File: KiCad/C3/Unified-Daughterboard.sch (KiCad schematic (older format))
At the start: 14 parts, among them J1 TYPE-C-31-M12_13, J2 SM04B-SRSS-TB(LF)(SN), U1 TPD4E05U06DQAR

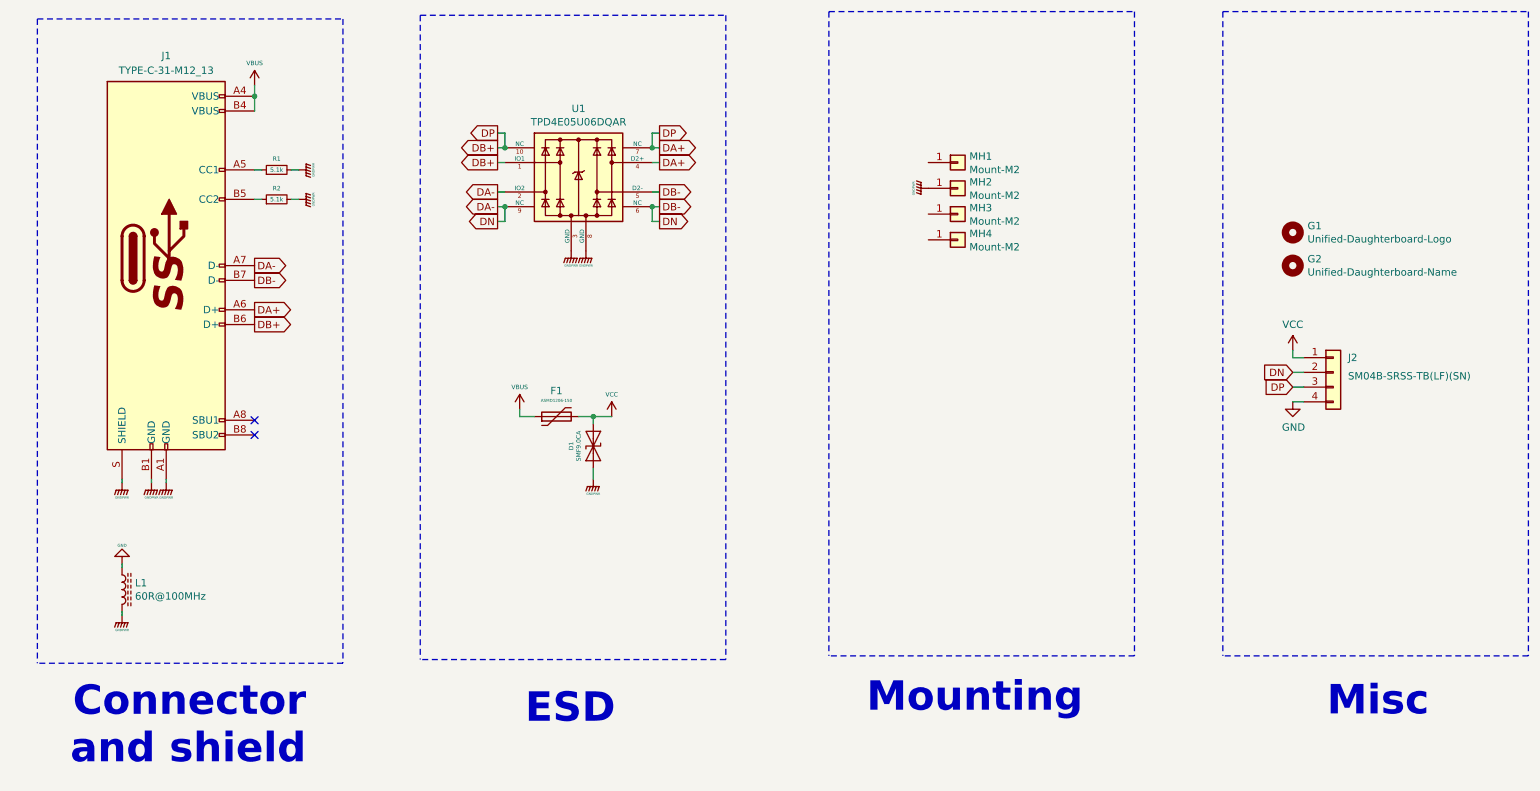
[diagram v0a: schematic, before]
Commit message: various optimizations to schematic and layout
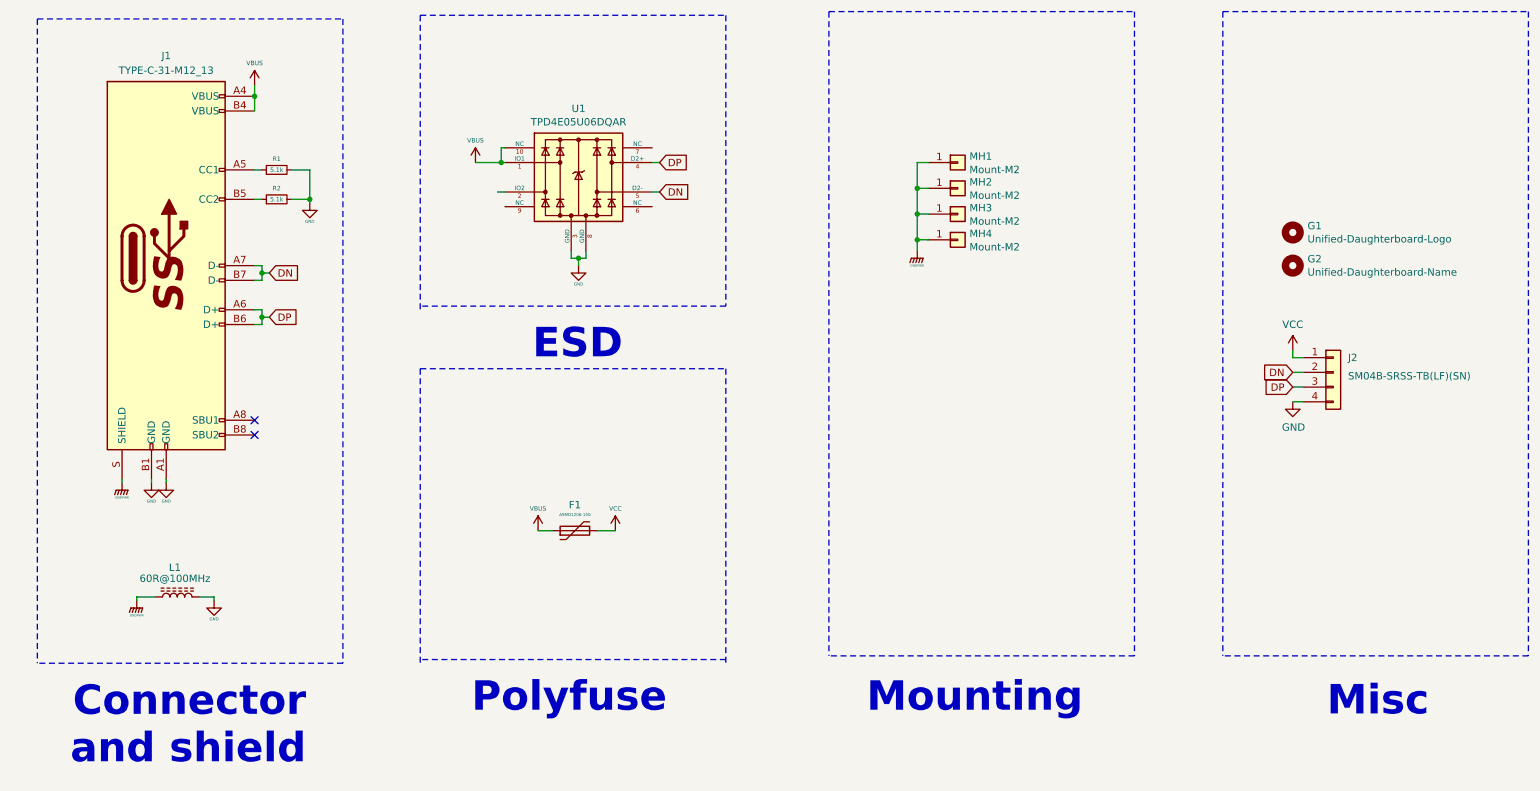
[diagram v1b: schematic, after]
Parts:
- removed D1: SMF9.0CA, acheron_Components:D_SOD-123_Bidirectional, symbol Device:D_TVS
- MH1, MH2, MH3, MH4: footprint random-keyboard-parts:Generic-Mounthole -> MountingHole:MountingHole_2.2mm_M2_ISO7380_Pad
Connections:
- net GND: now also J1.A1 (GND), J1.B1 (GND), L1.2, R1.2, R2.2, U1.3 (GND), U1.8 (GND); no longer L1.1
- net GNDPWR: now also L1.1, MH1.1 (Pin_1), MH3.1 (Pin_1), MH4.1 (Pin_1); no longer J1.A1 (GND), J1.B1 (GND), L1.2, R1.2, R2.2, U1.3 (GND), U1.8 (GND)
- net VBUS: now also U1.1 (IO1), U1.10 (NC)
- net DA+ renamed DP
- net DP: no longer U1.1 (IO1), U1.10 (NC), U1.7 (NC)
- net DA- renamed DN
- net DN: no longer U1.2 (IO2), U1.6 (NC), U1.9 (NC)
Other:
- note added: "Polyfuse"
- moved on the sheet: F1, L1
